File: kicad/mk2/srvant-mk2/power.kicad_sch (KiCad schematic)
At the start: 40 parts, among them J1 Barrel_Jack_Switch, U1 INA219AxDCN, U11 BSZ040N04LSGATMA1, U2 AP64501SP-13

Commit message: more progress
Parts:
- removed U11: BSZ040N04LSGATMA1, footprints:bsz086p03ns, symbol bsz086p03ns:BSZ040N04LSGATMA1
- added Q1: DMP3013SFV-7, Package_SON:Diodes_PowerDI3333-8, symbol Transistor_FET:DMP3013SFV
- J1: footprint (none) -> footprints:DC-jack-694106301002; manf# (none) -> 694106301002; mouser# (none) -> 710-694106301002
- R1: value R -> 12K; footprint (none) -> Resistor_SMD:R_0402_1005Metric
- R15, R16: footprint (none) -> Resistor_SMD:R_0402_1005Metric
- R17, R18: footprint (none) -> Resistor_SMD:R_0402_1005Metric; farnell# (none) -> 9238999; manf# (none) -> RC0402FR-0710RL
- TP1: footprint (none) -> TestPoint:TestPoint_Pad_D1.0mm
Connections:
- net at C1.1, C10.1, C2.1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: now also Q1.1 (S), Q1.2 (S), Q1.3 (S)
- net at C10.2, D1.2 (A), R1.1: now also Q1.4 (G)
- net at C7.1, J1.1: now also Q1.5 (D)
- net BMC_I2C_0_SCL renamed BMC_I2C_0_SCK
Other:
- note removed: "5v @ 3A PSU"
- moved on the sheet: C7, J1, TP3

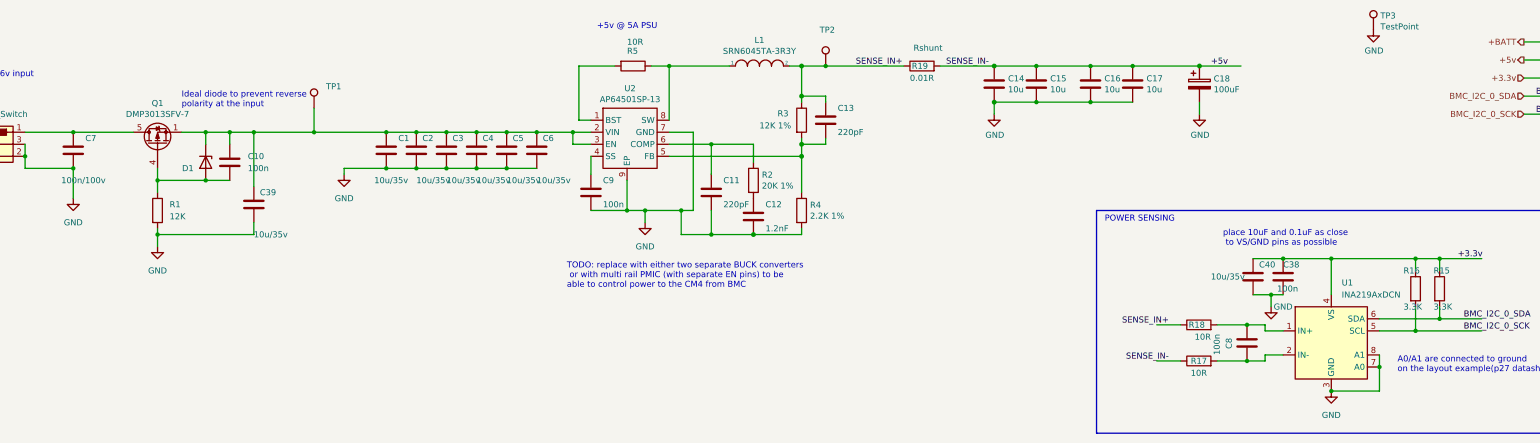
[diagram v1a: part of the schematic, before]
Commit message: merge cm4 into one page, basic interconnection
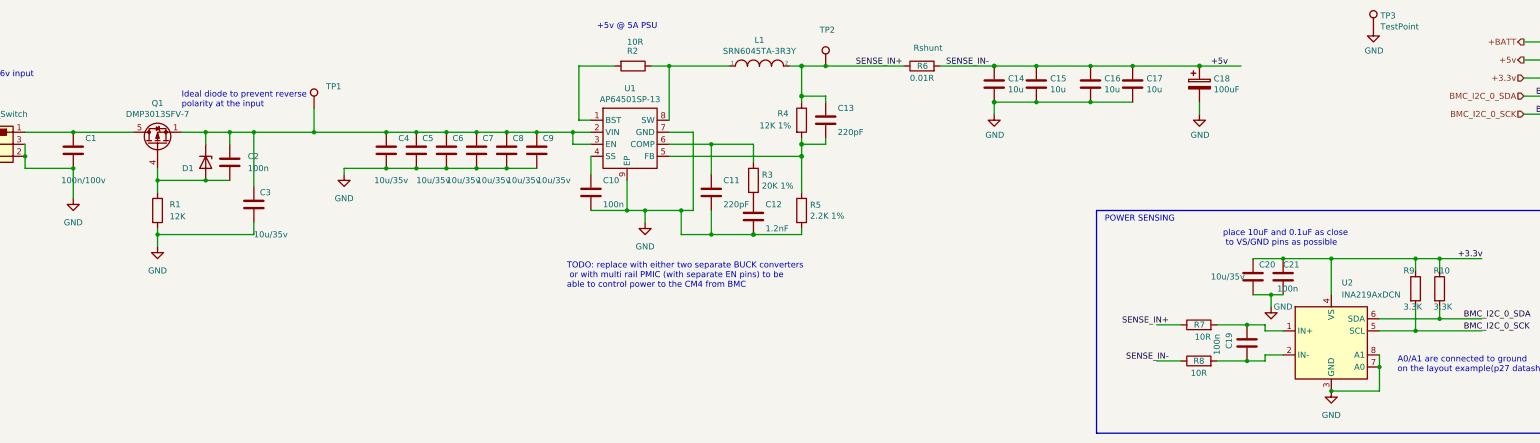
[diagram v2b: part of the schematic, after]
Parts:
- renumbered C7 to C1, C9 to C10, C8 to C19, C10 to C2, C40 to C20, C38 to C21, C39 to C3, C1 to C4, C2 to C5, C3 to C6, C4 to C7, C5 to C8, C6 to C9, R15 to R10, R5 to R2, R2 to R3, R3 to R4, R4 to R5, R19 to R6, R18 to R7, R17 to R8, R16 to R9, U2 to U1, U1 to U2

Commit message: more progress
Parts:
- removed R6: 0.01R, symbol Device:R
- added BT1: Battery_Cell, footprints:battery-S8411-45R, symbol Device:Battery_Cell
- added C10, C4, C6, C8: 10u/35v, Capacitor_SMD:C_0402_1005Metric, symbol Device:C
- added C15: 100n, Capacitor_SMD:C_0402_1005Metric, symbol Device:C
- added C18, C19, C21, C22: 10u, Capacitor_SMD:C_0805_2012Metric, symbol Device:C
- added C24: 100uF, Capacitor_Tantalum_SMD:CP_EIA-7343-31_Kemet-D, symbol Device:CP
- added D2: BAT54C-7-F, Package_TO_SOT_SMD:SOT-23, symbol Diode:BAT54C
- added J2: Conn_01x02, Connector_PinHeader_1.00mm:PinHeader_1x02_P1.00mm_Vertical, symbol Connector_Generic:Conn_01x02
- added L1: SRN4018-4R7M, Inductor_SMD:L_Bourns-SRN4018, symbol pspice:INDUCTOR
- added R2: 0.005R, Resistor_SMD:R_0805_2012Metric, symbol Device:R
- added U1: AP63205WU, Package_TO_SOT_SMD:TSOT-23-6, symbol Regulator_Switching:AP63205WU
- added U3: 74AHC1G32, Package_TO_SOT_SMD:SOT-23-5, symbol 74xGxx:74AHC1G32
- renumbered C7 to C11, C8 to C12, C9 to C13, C10 to C14, C11 to C16, C12 to C17, C13 to C20, C14 to C23, C15 to C25, C16 to C26, C17 to C27, C18 to C28, C19 to C29, C20 to C30, C21 to C31, C4 to C5, C5 to C7, C6 to C9, L1 to L2, R2 to R3, R3 to R4, R4 to R5, R5 to R6, U1 to U2, U2 to U4
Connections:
- net +BATT: now also D2.3
- net GND: now also BT1.2 (-), C10.2, C18.2, C19.2, C21.2, C22.2, C24.2, C4.2, C6.2, C8.2, U1.4 (GND), U3.3 (GND)
- net SENSE_IN+: now also C2.1, C3.1, D1.1 (K), Q1.1 (S), Q1.2 (S), Q1.3 (S), TP1.1, R2.1; no longer C20.1, L2.2, R5.1, TP2.1
- net +3.3v renamed +3.3v_BMC
- net +3.3v_BMC: now also D2.2, J2.2 (Pin_2), U3.5 (VCC)
- net +5v renamed +5v_HOST
- net +5v_HOST: now also C20.1, L2.2, R5.1, TP2.1; no longer R8.1
- new net: C15.2, L1.1, U1.5 (SW)
- new net: C15.1, U1.6 (BST)
- new net: J2.1 (Pin_1), U3.1
- new net: BT1.1 (+), D2.1
- new net +5v_BMC: C18.1, C19.1, C21.1, C22.1, C24.1, L1.2, U1.1 (FB)
- new net BMC_HOST_POWER_EN: U3.2
- new net PSU_EN: U2.3 (EN), U3.4
- new net SENSE_IN-: C10.1, C11.1, C12.1, C13.1, C4.1, C5.1, C6.1, C7.1, C8.1, C9.1, R2.2, R8.1, U1.2 (EN), U1.3 (IN), U2.2 (VIN)
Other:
- note added: "+5v @ 2A PSU"
- note added: "Host PSU should be enabled from/by the BMC For the dev period add a jumper and `OR gate` to be able to override the BMC and turn the power of the Host."
- note added: "Rshunt: * do the math, is 0.005 is OK? * what material is better? metal strip / metal alloy / thick film"
- note removed: "TODO: replace with either two separate BUCK converters or with multi rail PMIC (with separate EN pins) to be able to control power to the CM4 from BMC"
- moved on the sheet: C1, C11, C12, C13, C14, C16, C17, C2, C20, C23, C25, C26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

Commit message: save state
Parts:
- removed TP3: TestPoint, TestPoint:TestPoint_Pad_2.0x2.0mm, symbol Connector:TestPoint
- added C75, C77: 10u 35v, Capacitor_SMD:C_0805_2012Metric, symbol Device:C
- added C78, C79: 100n, Capacitor_SMD:C_0402_1005Metric, symbol Device:C
- added C83, C85, C87: 10u, Capacitor_SMD:C_0805_2012Metric, symbol Device:C
- added L3: SRN6045TA-3R3Y, Inductor_SMD:L_Bourns_SRN6045TA, symbol pspice:INDUCTOR
- added R55: 100K 1%, Resistor_SMD:R_0402_1005Metric, symbol Device:R
- added R56: 22K 1%, Resistor_SMD:R_0402_1005Metric, symbol Device:R
- added TP16: +5v BMC, TestPoint:TestPoint_Pad_D1.0mm, symbol Connector:TestPoint
- added TP6: VIN, TestPoint:TestPoint_Pad_D1.0mm, symbol ARJM11:TestPoint
- added U13: RT9742SNGV, Package_TO_SOT_SMD:SOT-23, symbol CM4IO:RT9742SNGV
- added U15: TLV62585DRLR, TLV62585DRLR:DRL0006A, symbol TLV62585DRLR:TLV62585DRLR
- TP1: value TestPoint (VIN) -> VIN
- TP2: value TestPoint -> +5v HOST
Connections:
- net +5v_BMC: now also TP16.1
- net +5v_HOST: now also C75.1, C77.1, C78.1, U13.1 (IN), U15.3 (VIN), U15.4 (EN)
- net GND: now also C75.2, C77.2, C78.2, C79.2, C83.2, C85.2, C87.2, R56.2, U13.3 (GND), U15.1 (GND)
- new net: L3.1, U15.2 (SW)
- new net +3.3v_HOST_PCIe: C83.1, C85.1, C87.1, L3.2, R55.1
- new net +5v_HOST_HDMI: C79.1, U13.2 (OUT)
- new net 3V3P_FB: R55.2, R56.1, TP6.1, U15.5 (FB)
- no-connect marks 0 -> 1
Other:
- note added: "3.3v @ 3A PSU For PCIE"
- note added: "Coin cell battery + BMC power rail are responsible for powering both RTC chips"
- note added: "HDMI power"
- note added: "PCIe power"
- moved on the sheet: BT1, D2, TP1

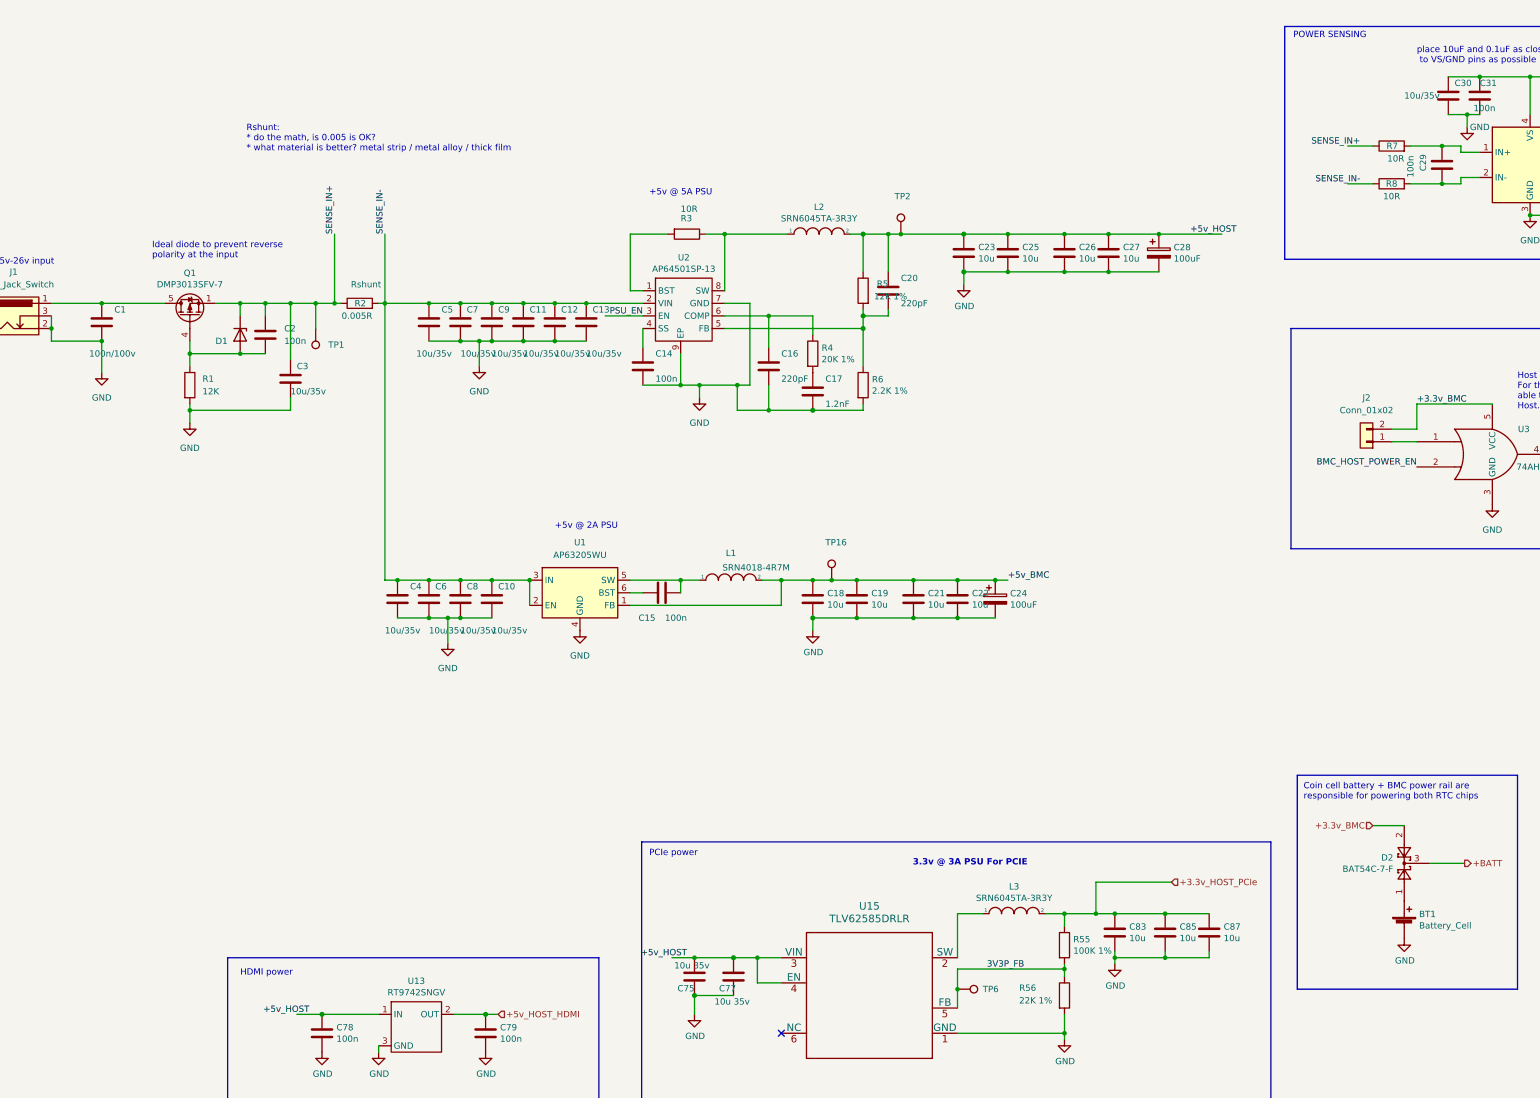
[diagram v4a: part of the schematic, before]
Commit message: fix descriptions, add 3dmodels.
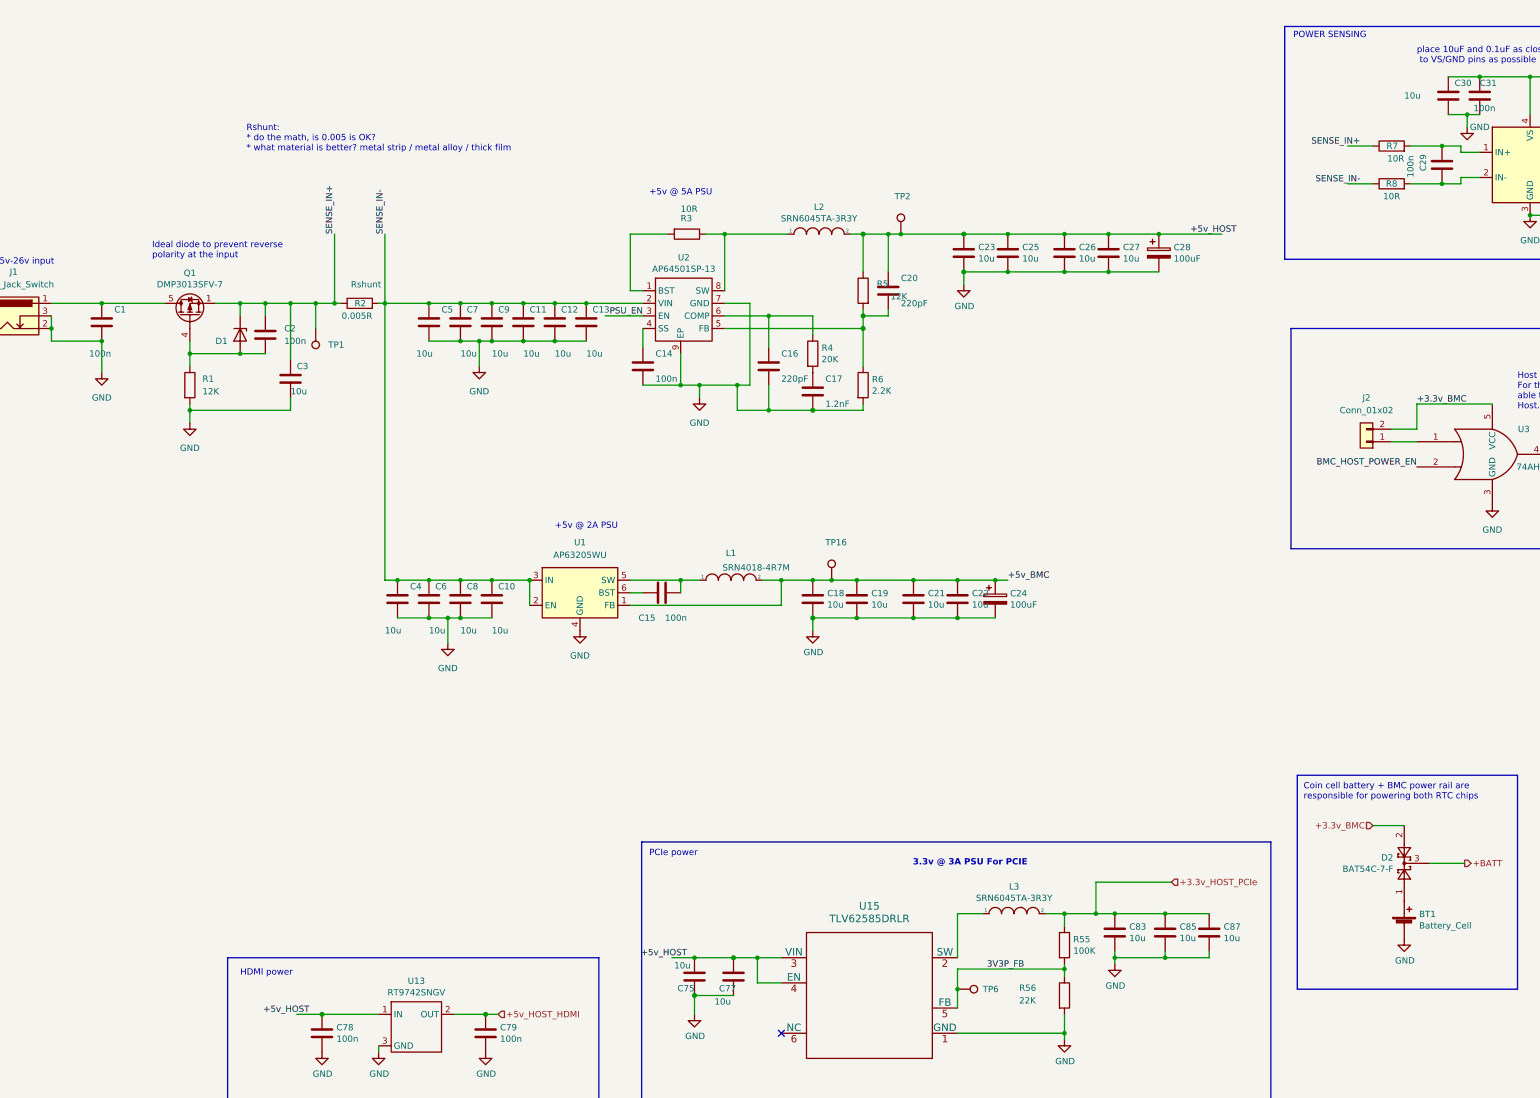
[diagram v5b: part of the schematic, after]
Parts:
- C1: value 100n/100v -> 100n
- C10, C11, C12, C13, C3, C30, C4, C5, C6, C7, C8, C9: value 10u/35v -> 10u
- C14, C15, C29, C78, C79: Part Description 0.1uF 10% 16V Ceramic Capacitor X7R 0402 (1005 Metric) -> 0.1uF 10% 16V Ceramic Capacitor X7R 0402 (1005 Metric)
- C18, C19, C21, C22, C23, C25, C26, C27, C83, C85, C87: Part Description 10uF 10% 10V Ceramic Capacitor X7R 0805 (2012 Metric) -> 10uF 10% 10V Ceramic Capacitor X7R 0805 (2012 Metric)
- C75, C77: value 10u 35v -> 10u; Part Description 10uF 10% or 20% 35V Ceramic Capacitor X6S 0805 (2012 Metric) -> 10uF 10% or 20% 35V Ceramic Capacitor X6S 0805 (2012 Metric)
- J1: footprint footprints:DC-jack-694106301002 -> Connector_BarrelJack:BarrelJack_Horizontal
- R4: value 20K 1% -> 20K
- R5: value 12K 1% -> 12K
- R55: value 100K 1% -> 100K
- R56: value 22K 1% -> 22K
- R6: value 2.2K 1% -> 2.2K
